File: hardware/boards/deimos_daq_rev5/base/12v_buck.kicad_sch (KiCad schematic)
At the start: 11 parts, among them IC12001 TPS560430XDBVR

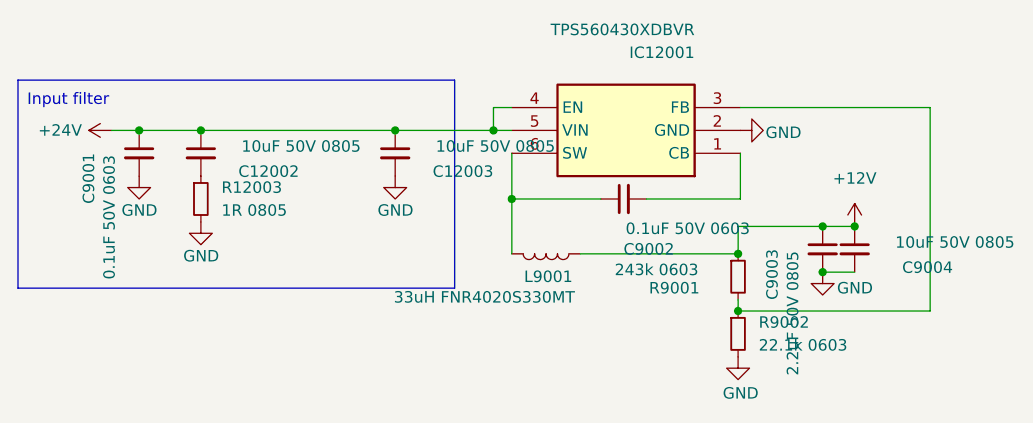
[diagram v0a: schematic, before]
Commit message: use opa196 with split rail instead of opa333 with single rail. replace zeners.
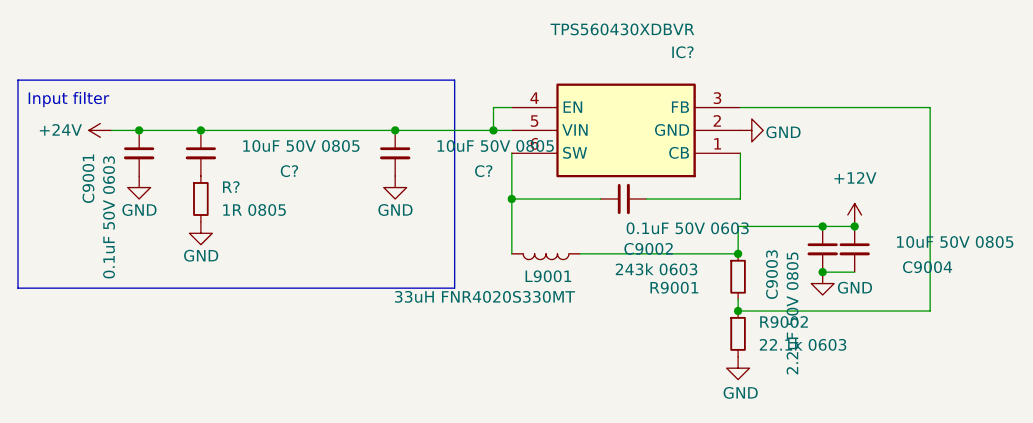
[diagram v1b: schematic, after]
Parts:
- renumbered C12003 to C?, C12002 to C?, IC12001 to IC?, R12003 to R?
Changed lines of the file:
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@@
 		(on_board yes)
 		(dnp no)
-		(property "Reference" "#PWR012002"
+		(property "Reference" "#PWR?"
 			(at 75.946 102.616 0)
 			(effects
@@
 		(pin "1"
 		)
+		(instances
+			(project "stm32h7_base"
+				(path "/511605a4-f92c-43a6-a2c6-3cb535ac8a8e/b0b0bf52-ab0f-447d-a4ad-06c08cf2163a"
+					(reference "#PWR?")
+					(unit 1)
+				)
+			)
+		)
 	)
 	(symbol
@@
 		(on_board yes)
 		(dnp no)
-		(property "Reference" "IC12001"
+		(property "Reference" "IC?"
 			(at 137.668 82.55 0)
 			(effects
@@
 		(pin "1"
 		)
+		(instances
+			(project "stm32h7_base"
+				(path "/511605a4-f92c-43a6-a2c6-3cb535ac8a8e/b0b0bf52-ab0f-447d-a4ad-06c08cf2163a"
+					(reference "IC?")
+					(unit 1)
+				)
+			)
+		)
 	)
 	(symbol
@@
 		(on_board yes)
 		(dnp no)
-		(property "Reference" "#PWR012008"
+		(property "Reference" "#PWR?"
 			(at 104.394 102.616 0)
 			(effects
@@
 		)
 		(pin "1"
+		)
+		(instances
+			(project "stm32h7_base"
+				(path "/511605a4-f92c-43a6-a2c6-3cb535ac8a8e/b0b0bf52-ab0f-447d-a4ad-06c08cf2163a"
+					(reference "#PWR?")
+					(unit 1)
+				)
+			)
 		)
 	)
@@
 		(on_board yes)
 		(dnp no)
-		(property "Reference" "C12003"
+		(property "Reference" "C?"
 			(at 115.316 95.758 0)
 			(effects
@@
 		)
 		(pin "2"
+		)
+		(instances
+			(project "stm32h7_base"
+				(path "/511605a4-f92c-43a6-a2c6-3cb535ac8a8e/b0b0bf52-ab0f-447d-a4ad-06c08cf2163a"
+					(reference "C?")
+					(unit 1)
+				)
+			)
 		)
 	)
@@
 		(on_board yes)
 		(dnp no)
-		(property "Reference" "C12002"
+		(property "Reference" "C?"
 			(at 93.726 95.758 0)
 			(effects
@@
 		(pin "2"
 		)
+		(instances
+			(project "stm32h7_base"
+				(path "/511605a4-f92c-43a6-a2c6-3cb535ac8a8e/b0b0bf52-ab0f-447d-a4ad-06c08cf2163a"
+					(reference "C?")
+					(unit 1)
+				)
+			)
+		)
 	)
 	(symbol
@@
 		(on_board yes)
 		(dnp no)
-		(property "Reference" "#PWR012004"
+		(property "Reference" "#PWR?"
 			(at 149.098 91.186 0)
 			(effects
@@
 		(pin "1"
 		)
+		(instances
+			(project "stm32h7_base"
+				(path "/511605a4-f92c-43a6-a2c6-3cb535ac8a8e/b0b0bf52-ab0f-447d-a4ad-06c08cf2163a"
+					(reference "#PWR?")
+					(unit 1)
+				)
+			)
+		)
 	)
 	(symbol
@@
 		(on_board yes)
 		(dnp no)
-		(property "Reference" "#PWR012005"
+		(property "Reference" "#PWR?"
 			(at 151.892 113.284 0)
 			(effects
@@
 		(pin "1"
 		)
+		(instances
+			(project "stm32h7_base"
+				(path "/511605a4-f92c-43a6-a2c6-3cb535ac8a8e/b0b0bf52-ab0f-447d-a4ad-06c08cf2163a"
+					(reference "#PWR?")
+					(unit 1)
+				)
+			)
+		)
 	)
 	(symbol
@@
 		(dnp no)
 		(fields_autoplaced yes)
-		(property "Reference" "#PWR012006"
+		(property "Reference" "#PWR?"
 			(at 155.448 105.664 0)
 			(effects
@@
 		(pin "1"
 		)
+		(instances
+			(project "stm32h7_base"
+				(path "/511605a4-f92c-43a6-a2c6-3cb535ac8a8e/b0b0bf52-ab0f-447d-a4ad-06c08cf2163a"
+					(reference "#PWR?")
+					(unit 1)
+				)
+			)
+		)
 	)
 	(symbol
@@
 		(on_board yes)
 		(dnp no)
-		(property "Reference" "#PWR012003"
+		(property "Reference" "#PWR?"
 			(at 142.494 122.682 0)
 			(effects
@@
 		(pin "1"
 		)
+		(instances
+			(project "stm32h7_base"
+				(path "/511605a4-f92c-43a6-a2c6-3cb535ac8a8e/b0b0bf52-ab0f-447d-a4ad-06c08cf2163a"
+					(reference "#PWR?")
+					(unit 1)
+				)
+			)
+		)
 	)
 	(symbol
@@
 		(dnp no)
 		(fields_autoplaced yes)
-		(property "Reference" "#PWR012001"
+		(property "Reference" "#PWR?"
 			(at 76.708 91.186 0)
 			(effects
@@
 		(pin "1"
 		)
+		(instances
+			(project "stm32h7_base"
+				(path "/511605a4-f92c-43a6-a2c6-3cb535ac8a8e/b0b0bf52-ab0f-447d-a4ad-06c08cf2163a"
+					(reference "#PWR?")
+					(unit 1)
+				)
+			)
+		)
 	)
 	(symbol
@@
 		(on_board yes)
 		(dnp no)
-		(property "Reference" "#PWR012007"
+		(property "Reference" "#PWR?"
 			(at 82.804 107.696 0)
 			(effects
@@
 		)
 		(pin "1"
+		)
+		(instances
+			(project "stm32h7_base"
+				(path "/511605a4-f92c-43a6-a2c6-3cb535ac8a8e/b0b0bf52-ab0f-447d-a4ad-06c08cf2163a"
+					(reference "#PWR?")
+					(unit 1)
+				)
+			)
 		)
 	)
@@
 		(dnp no)
 		(fields_autoplaced yes)
-		(property "Reference" "R12003"
+		(property "Reference" "R?"
 			(at 85.09 97.5359 0)
 			(effects
@@
 		(pin "2"
 		)
-	)
+		(instances
+			(project "stm32h7_base"
+				(path "/511605a4-f92c-43a6-a2c6-3cb535ac8a8e/b0b0bf52-ab0f-447d-a4ad-06c08cf2163a"
+					(reference "R?")
+					(unit 1)
+				)
+			)
+		)
+	)

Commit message: wip to update layout for controller base
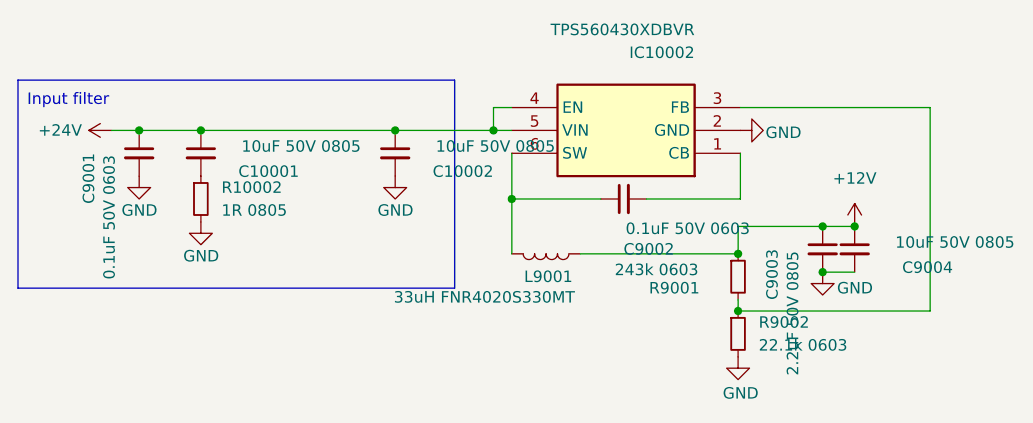
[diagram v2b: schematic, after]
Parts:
- gave numbers to parts that had none: 4
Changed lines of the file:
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@@
 		(on_board yes)
 		(dnp no)
-		(property "Reference" "#PWR?"
+		(property "Reference" "#PWR118"
 			(at 75.946 102.616 0)
 			(effects
@@
 			(project "stm32h7_base"
 				(path "/511605a4-f92c-43a6-a2c6-3cb535ac8a8e/b0b0bf52-ab0f-447d-a4ad-06c08cf2163a"
-					(reference "#PWR?")
+					(reference "#PWR118")
 					(unit 1)
 				)
@@
 		(on_board yes)
 		(dnp no)
-		(property "Reference" "IC?"
+		(property "Reference" "IC10002"
 			(at 137.668 82.55 0)
 			(effects
@@
 			(project "stm32h7_base"
 				(path "/511605a4-f92c-43a6-a2c6-3cb535ac8a8e/b0b0bf52-ab0f-447d-a4ad-06c08cf2163a"
-					(reference "IC?")
+					(reference "IC10002")
 					(unit 1)
 				)
@@
 		(on_board yes)
 		(dnp no)
-		(property "Reference" "#PWR?"
+		(property "Reference" "#PWR115"
 			(at 104.394 102.616 0)
 			(effects
@@
 			(project "stm32h7_base"
 				(path "/511605a4-f92c-43a6-a2c6-3cb535ac8a8e/b0b0bf52-ab0f-447d-a4ad-06c08cf2163a"
-					(reference "#PWR?")
+					(reference "#PWR115")
 					(unit 1)
 				)
@@
 		(on_board yes)
 		(dnp no)
-		(property "Reference" "C?"
+		(property "Reference" "C10002"
 			(at 115.316 95.758 0)
 			(effects
@@
 			(project "stm32h7_base"
 				(path "/511605a4-f92c-43a6-a2c6-3cb535ac8a8e/b0b0bf52-ab0f-447d-a4ad-06c08cf2163a"
-					(reference "C?")
+					(reference "C10002")
 					(unit 1)
 				)
@@
 		(on_board yes)
 		(dnp no)
-		(property "Reference" "C?"
+		(property "Reference" "C10001"
 			(at 93.726 95.758 0)
 			(effects
@@
 			(project "stm32h7_base"
 				(path "/511605a4-f92c-43a6-a2c6-3cb535ac8a8e/b0b0bf52-ab0f-447d-a4ad-06c08cf2163a"
-					(reference "C?")
+					(reference "C10001")
 					(unit 1)
 				)
@@
 		(on_board yes)
 		(dnp no)
-		(property "Reference" "#PWR?"
+		(property "Reference" "#PWR113"
 			(at 149.098 91.186 0)
 			(effects
@@
 			(project "stm32h7_base"
 				(path "/511605a4-f92c-43a6-a2c6-3cb535ac8a8e/b0b0bf52-ab0f-447d-a4ad-06c08cf2163a"
-					(reference "#PWR?")
+					(reference "#PWR113")
 					(unit 1)
 				)
@@
 		(on_board yes)
 		(dnp no)
-		(property "Reference" "#PWR?"
+		(property "Reference" "#PWR112"
 			(at 151.892 113.284 0)
 			(effects
@@
 			(project "stm32h7_base"
 				(path "/511605a4-f92c-43a6-a2c6-3cb535ac8a8e/b0b0bf52-ab0f-447d-a4ad-06c08cf2163a"
-					(reference "#PWR?")
+					(reference "#PWR112")
 					(unit 1)
 				)
@@
 		(dnp no)
 		(fields_autoplaced yes)
-		(property "Reference" "#PWR?"
+		(property "Reference" "#PWR111"
 			(at 155.448 105.664 0)
 			(effects
@@
 			(project "stm32h7_base"
 				(path "/511605a4-f92c-43a6-a2c6-3cb535ac8a8e/b0b0bf52-ab0f-447d-a4ad-06c08cf2163a"
-					(reference "#PWR?")
+					(reference "#PWR111")
 					(unit 1)
 				)
@@
 		(on_board yes)
 		(dnp no)
-		(property "Reference" "#PWR?"
+		(property "Reference" "#PWR114"
 			(at 142.494 122.682 0)
 			(effects
@@
 			(project "stm32h7_base"
 				(path "/511605a4-f92c-43a6-a2c6-3cb535ac8a8e/b0b0bf52-ab0f-447d-a4ad-06c08cf2163a"
-					(reference "#PWR?")
+					(reference "#PWR114")
 					(unit 1)
 				)
@@
 		(dnp no)
 		(fields_autoplaced yes)
-		(property "Reference" "#PWR?"
+		(property "Reference" "#PWR116"
 			(at 76.708 91.186 0)
 			(effects
@@
 			(project "stm32h7_base"
 				(path "/511605a4-f92c-43a6-a2c6-3cb535ac8a8e/b0b0bf52-ab0f-447d-a4ad-06c08cf2163a"
-					(reference "#PWR?")
+					(reference "#PWR116")
 					(unit 1)
 				)
@@
 		(on_board yes)
 		(dnp no)
-		(property "Reference" "#PWR?"
+		(property "Reference" "#PWR117"
 			(at 82.804 107.696 0)
 			(effects
@@
 			(project "stm32h7_base"
 				(path "/511605a4-f92c-43a6-a2c6-3cb535ac8a8e/b0b0bf52-ab0f-447d-a4ad-06c08cf2163a"
-					(reference "#PWR?")
+					(reference "#PWR117")
 					(unit 1)
 				)
@@
 		(dnp no)
 		(fields_autoplaced yes)
-		(property "Reference" "R?"
+		(property "Reference" "R10002"
 			(at 85.09 97.5359 0)
 			(effects
@@
 			(project "stm32h7_base"
 				(path "/511605a4-f92c-43a6-a2c6-3cb535ac8a8e/b0b0bf52-ab0f-447d-a4ad-06c08cf2163a"
-					(reference "R?")
-					(unit 1)
-				)
+					(reference "R10002")
+					(unit 1)
+				)

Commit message: restore rev5 and make this rev rev6
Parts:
- renumbered C10001 to C12002, C10002 to C12003, IC10002 to IC12001, R10002 to R12003
